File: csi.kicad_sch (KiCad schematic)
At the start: 0 parts

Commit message: Schematic cleanup
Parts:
- added J?: WE_68715014522, antmicro-footprints:WE_68715014522, symbol antmicroFCCConnectors:WE_68715014522
- added MP? (x4): PCB_Mount_Hole_4.3_NPTH, antmicro-footprints:mounting-hole-4.2mm-NPTH, symbol antmicroMechanicalParts:PCB_Mount_Hole_4.3_NPTH
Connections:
- new net +3V3: J?.47 (Pin_47), J?.48 (Pin_48)
- new net +5V: J?.49 (Pin_49), J?.50 (Pin_50)
- new net CSI1_CLK_N: J?.28 (Pin_28)
- new net CSI1_CLK_P: J?.29 (Pin_29)
- new net CSI1_D1_N: J?.25 (Pin_25)
- new net CSI1_D1_P: J?.26 (Pin_26)
- new net CSI1_D2_N: J?.23 (Pin_23)
- new net CSI1_D2_P: J?.24 (Pin_24)
- new net CSI1_D3_N: J?.21 (Pin_21)
- new net CSI1_D3_P: J?.22 (Pin_22)
- new net CSI1_D4_N: J?.19 (Pin_19)
- new net CSI1_D4_P: J?.20 (Pin_20)
- new net CSI2_CLK_N: J?.13 (Pin_13)
- new net CSI2_CLK_P: J?.14 (Pin_14)
- new net CSI2_D1_N: J?.16 (Pin_16)
- new net CSI2_D1_P: J?.17 (Pin_17)
- new net CSI3_CLK_N: J?.10 (Pin_10)
- new net CSI3_CLK_P: J?.11 (Pin_11)
- new net CSI3_D1_N: J?.7 (Pin_7)
- new net CSI3_D1_P: J?.8 (Pin_8)
- new net CSI3_D2_N: J?.5 (Pin_5)
- new net CSI3_D2_P: J?.6 (Pin_6)
- new net CSI3_D3_N: J?.3 (Pin_3)
- new net CSI3_D3_P: J?.4 (Pin_4)
- new net CSI3_D4_N: J?.1 (Pin_1)
- new net CSI3_D4_P: J?.2 (Pin_2)
- new net GND: J?.12 (Pin_12), J?.15 (Pin_15), J?.18 (Pin_18), J?.9 (Pin_9)
- new net GPIO1: J?.31 (Pin_31)
- new net GPIO2: J?.32 (Pin_32)
- new net GPIO3: J?.33 (Pin_33)
- new net GPIO4: J?.34 (Pin_34)
- new net I2C1_SCL: J?.42 (Pin_42)
- new net I2C1_SDA: J?.41 (Pin_41)
- new net I2C3_SCL: J?.40 (Pin_40)
- new net I2C3_SDA: J?.39 (Pin_39)
- new net SPI_CS: J?.46 (Pin_46)
- new net SPI_MISO: J?.44 (Pin_44)
- new net SPI_MOSI: J?.45 (Pin_45)
- new net SPI_SCK: J?.43 (Pin_43)
- new net UART3_RX: J?.36 (Pin_36)
- new net UART3_TX: J?.35 (Pin_35)
- new net UART4_RX: J?.38 (Pin_38)
- new net UART4_TX: J?.37 (Pin_37)
- no-connect marks 0 -> 16
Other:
- removed sheet CSI
- removed sheet Channel 1
- removed sheet Channel 2
- note added: "Camera board connector"
- note added: "The connector has flipped pads on the PCB"
- note added: "To make it compatible with TK1, TX1 boards"
- title: Antmicro HDMI MIPI Bridge -> (none)

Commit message: Updated components
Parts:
- removed J?: WE_68715014522, antmicro-footprints:WE_68715014522, symbol antmicroFCCConnectors:WE_68715014522
- added J6: WE_68715014022, antmicro-footprints:WE_68715014022, symbol antmicroFCCConnectors:WE_68715014022
- gave numbers to parts that had none: 4
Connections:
- net +3V3: now also J6.47 (Pin_47), J6.48 (Pin_48)
- net +5V: now also J6.49 (Pin_49), J6.50 (Pin_50)
- net CSI1_CLK_N: now also J6.28 (Pin_28)
- net CSI1_CLK_P: now also J6.29 (Pin_29)
- net CSI1_D1_N: now also J6.25 (Pin_25)
- net CSI1_D1_P: now also J6.26 (Pin_26)
- net CSI1_D2_N: now also J6.23 (Pin_23)
- net CSI1_D2_P: now also J6.24 (Pin_24)
- net CSI1_D3_N: now also J6.21 (Pin_21)
- net CSI1_D3_P: now also J6.22 (Pin_22)
- net CSI1_D4_N: now also J6.19 (Pin_19)
- net CSI1_D4_P: now also J6.20 (Pin_20)
- net CSI2_CLK_N: now also J6.13 (Pin_13)
- net CSI2_CLK_P: now also J6.14 (Pin_14)
- net CSI2_D1_N: now also J6.16 (Pin_16)
- net CSI2_D1_P: now also J6.17 (Pin_17)
- net CSI3_CLK_N: now also J6.10 (Pin_10)
- net CSI3_CLK_P: now also J6.11 (Pin_11)
- net CSI3_D1_N: now also J6.7 (Pin_7)
- net CSI3_D1_P: now also J6.8 (Pin_8)
- net CSI3_D2_N: now also J6.5 (Pin_5)
- net CSI3_D2_P: now also J6.6 (Pin_6)
- net CSI3_D3_N: now also J6.3 (Pin_3)
- net CSI3_D3_P: now also J6.4 (Pin_4)
- net CSI3_D4_N: now also J6.1 (Pin_1)
- net CSI3_D4_P: now also J6.2 (Pin_2)
- net GND: now also J6.12 (Pin_12), J6.15 (Pin_15), J6.18 (Pin_18), J6.9 (Pin_9)
- net GPIO1: now also J6.31 (Pin_31)
- net GPIO2: now also J6.32 (Pin_32)
- net GPIO3: now also J6.33 (Pin_33)
- net GPIO4: now also J6.34 (Pin_34)
- net I2C1_SCL: now also J6.42 (Pin_42)
- net I2C1_SDA: now also J6.41 (Pin_41)
- net I2C3_SCL: now also J6.40 (Pin_40)
- net I2C3_SDA: now also J6.39 (Pin_39)
- net SPI_CS: now also J6.46 (Pin_46)
- net SPI_MISO: now also J6.44 (Pin_44)
- net SPI_MOSI: now also J6.45 (Pin_45)
- net SPI_SCK: now also J6.43 (Pin_43)
- net UART3_RX: now also J6.36 (Pin_36)
- net UART3_TX: now also J6.35 (Pin_35)
- net UART4_RX: now also J6.38 (Pin_38)
- net UART4_TX: now also J6.37 (Pin_37)
- no-connect marks 16 -> 18
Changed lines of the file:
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@@
   (no_connect (at 186.69 189.23))
   (no_connect (at 186.69 113.03))
+  (no_connect (at 204.47 156.21))
+  (no_connect (at 204.47 148.59))
   (wire (pts (xy 203.2 207.01) (xy 204.47 207.01))
     (stroke (width 0) (type default) (color 0 0 0 0))
@@
     )
   )
-  (symbol (lib_id "antmicroFCCConnectors:WE_68715014522") (at 209.55 123.19 0) (unit 1)
+  (symbol (lib_id "antmicroMechanicalParts:PCB_Mount_Hole_4.3_NPTH") (at 297.18 205.74 0) (unit 1)
     (in_bom yes) (on_board yes) (fields_autoplaced)
-    (property "Reference" "J?" (id 0) (at 212.09 143.5099 0)
+    (property "Reference" "MP4" (id 0) (at 303.53 204.4699 0)
       (effects (font (size 1.27 1.27)) (justify left))
     )
-    (property "Value" "WE_68715014522" (id 1) (at 212.09 146.0499 0)
+    (property "Value" "PCB_Mount_Hole_4.3_NPTH" (id 1) (at 303.53 207.0099 0)
       (effects (font (size 1.27 1.27)) (justify left))
     )
-    (property "Footprint" "antmicro-footprints:WE_68715014522" (id 2) (at 204.47 213.36 0)
+    (property "Footprint" "antmicro-footprints:mounting-hole-4.2mm-NPTH" (id 2) (at 297.18 195.58 0)
       (effects (font (size 1.27 1.27)) hide)
     )
-    (property "Datasheet" "https://katalog.we-online.de/em/datasheet/6871xx14522.pdf" (id 3) (at 209.55 215.9 0)
+    (property "Datasheet" "" (id 3) (at 321.31 185.42 0)
       (effects (font (size 1.27 1.27)) hide)
     )
-    (property "MPN" "68715014522 " (id 4) (at 219.71 138.43 0)
+  )
+  (symbol (lib_id "antmicroMechanicalParts:PCB_Mount_Hole_4.3_NPTH") (at 259.08 205.74 0) (unit 1)
+    (in_bom yes) (on_board yes) (fields_autoplaced)
+    (property "Reference" "MP2" (id 0) (at 265.43 204.4699 0)
+      (effects (font (size 1.27 1.27)) (justify left))
+    )
+    (property "Value" "PCB_Mount_Hole_4.3_NPTH" (id 1) (at 265.43 207.0099 0)
+      (effects (font (size 1.27 1.27)) (justify left))
+    )
+    (property "Footprint" "antmicro-footprints:mounting-hole-4.2mm-NPTH" (id 2) (at 259.08 195.58 0)
+      (effects (font (size 1.27 1.27)) hide)
+    )
+    (property "Datasheet" "" (id 3) (at 283.21 185.42 0)
+      (effects (font (size 1.27 1.27)) hide)
+    )
+  )
+  (symbol (lib_id "antmicroMechanicalParts:PCB_Mount_Hole_4.3_NPTH") (at 259.08 195.58 0) (unit 1)
+    (in_bom yes) (on_board yes) (fields_autoplaced)
+    (property "Reference" "MP1" (id 0) (at 265.43 194.3099 0)
+      (effects (font (size 1.27 1.27)) (justify left))
+    )
+    (property "Value" "PCB_Mount_Hole_4.3_NPTH" (id 1) (at 265.43 196.8499 0)
+      (effects (font (size 1.27 1.27)) (justify left))
+    )
+    (property "Footprint" "antmicro-footprints:mounting-hole-4.2mm-NPTH" (id 2) (at 259.08 185.42 0)
+      (effects (font (size 1.27 1.27)) hide)
+    )
+    (property "Datasheet" "" (id 3) (at 283.21 175.26 0)
+      (effects (font (size 1.27 1.27)) hide)
+    )
+  )
+  (symbol (lib_id "power:GND") (at 201.93 209.55 0) (unit 1)
+    (in_bom yes) (on_board yes) (fields_autoplaced)
+    (property "Reference" "#PWR0101" (id 0) (at 201.93 215.9 0)
+      (effects (font (size 1.27 1.27)) hide)
+    )
+    (property "Value" "GND" (id 1) (at 201.93 214.63 0))
+    (property "Footprint" "" (id 2) (at 201.93 209.55 0)
+      (effects (font (size 1.27 1.27)) hide)
+    )
+    (property "Datasheet" "" (id 3) (at 201.93 209.55 0)
+      (effects (font (size 1.27 1.27)) hide)
+    )
+    (pin "1")
+  )
+  (symbol (lib_id "antmicroMechanicalParts:PCB_Mount_Hole_4.3_NPTH") (at 297.18 195.58 0) (unit 1)
+    (in_bom yes) (on_board yes) (fields_autoplaced)
+    (property "Reference" "MP3" (id 0) (at 303.53 194.3099 0)
+      (effects (font (size 1.27 1.27)) (justify left))
+    )
+    (property "Value" "PCB_Mount_Hole_4.3_NPTH" (id 1) (at 303.53 196.8499 0)
+      (effects (font (size 1.27 1.27)) (justify left))
+    )
+    (property "Footprint" "antmicro-footprints:mounting-hole-4.2mm-NPTH" (id 2) (at 297.18 185.42 0)
+      (effects (font (size 1.27 1.27)) hide)
+    )
+    (property "Datasheet" "" (id 3) (at 321.31 175.26 0)
+      (effects (font (size 1.27 1.27)) hide)
+    )
+  )
+  (symbol (lib_id "power:+3V3") (at 198.12 200.66 0) (unit 1)
+    (in_bom yes) (on_board yes)
+    (property "Reference" "#PWR0102" (id 0) (at 198.12 204.47 0)
+      (effects (font (size 1.27 1.27)) hide)
+    )
+    (property "Value" "+3V3" (id 1) (at 194.31 199.39 0))
+    (property "Footprint" "" (id 2) (at 198.12 200.66 0)
+      (effects (font (size 1.27 1.27)) hide)
+    )
+    (property "Datasheet" "" (id 3) (at 198.12 200.66 0)
+      (effects (font (size 1.27 1.27)) hide)
+    )
+    (pin "1")
+  )
+  (symbol (lib_id "antmicroFCCConnectors:WE_68715014022") (at 209.55 123.19 0) (unit 1)
+    (in_bom yes) (on_board yes) (fields_autoplaced)
+    (property "Reference" "J6" (id 0) (at 212.09 143.5099 0)
+      (effects (font (size 1.27 1.27)) (justify left))
+    )
+    (property "Value" "WE_68715014022" (id 1) (at 212.09 146.0499 0)
+      (effects (font (size 1.27 1.27)) (justify left))
+    )
+    (property "Footprint" "antmicro-footprints:WE_68715014022" (id 2) (at 204.47 213.36 0)
+      (effects (font (size 1.27 1.27)) hide)
+    )
+    (property "Datasheet" "" (id 3) (at 209.55 215.9 0)
+      (effects (font (size 1.27 1.27)) hide)
+    )
+    (property "MPN" "68715014022 " (id 4) (at 219.71 138.43 0)
       (effects (font (size 1.524 1.524)) (justify left) hide)
     )
@@
     (pin "9")
   )
-  (symbol (lib_id "antmicroMechanicalParts:PCB_Mount_Hole_4.3_NPTH") (at 297.18 205.74 0) (unit 1)
-    (in_bom yes) (on_board yes) (fields_autoplaced)
-    (property "Reference" "MP?" (id 0) (at 303.53 204.4699 0)
-      (effects (font (size 1.27 1.27)) (justify left))
-    )
-    (property "Value" "PCB_Mount_Hole_4.3_NPTH" (id 1) (at 303.53 207.0099 0)
-      (effects (font (size 1.27 1.27)) (justify left))
-    )
-    (property "Footprint" "antmicro-footprints:mounting-hole-4.2mm-NPTH" (id 2) (at 297.18 195.58 0)
-      (effects (font (size 1.27 1.27)) hide)
-    )
-    (property "Datasheet" "" (id 3) (at 321.31 185.42 0)
-      (effects (font (size 1.27 1.27)) hide)
-    )
-  )
-  (symbol (lib_id "antmicroMechanicalParts:PCB_Mount_Hole_4.3_NPTH") (at 259.08 205.74 0) (unit 1)
-    (in_bom yes) (on_board yes) (fields_autoplaced)
-    (property "Reference" "MP?" (id 0) (at 265.43 204.4699 0)
-      (effects (font (size 1.27 1.27)) (justify left))
-    )
-    (property "Value" "PCB_Mount_Hole_4.3_NPTH" (id 1) (at 265.43 207.0099 0)
-      (effects (font (size 1.27 1.27)) (justify left))
-    )
-    (property "Footprint" "antmicro-footprints:mounting-hole-4.2mm-NPTH" (id 2) (at 259.08 195.58 0)
-      (effects (font (size 1.27 1.27)) hide)
-    )
-    (property "Datasheet" "" (id 3) (at 283.21 185.42 0)
-      (effects (font (size 1.27 1.27)) hide)
-    )
-  )
-  (symbol (lib_id "antmicroMechanicalParts:PCB_Mount_Hole_4.3_NPTH") (at 259.08 195.58 0) (unit 1)
-    (in_bom yes) (on_board yes) (fields_autoplaced)
-    (property "Reference" "MP?" (id 0) (at 265.43 194.3099 0)
-      (effects (font (size 1.27 1.27)) (justify left))
-    )
-    (property "Value" "PCB_Mount_Hole_4.3_NPTH" (id 1) (at 265.43 196.8499 0)
-      (effects (font (size 1.27 1.27)) (justify left))
-    )
-    (property "Footprint" "antmicro-footprints:mounting-hole-4.2mm-NPTH" (id 2) (at 259.08 185.42 0)
-      (effects (font (size 1.27 1.27)) hide)
-    )
-    (property "Datasheet" "" (id 3) (at 283.21 175.26 0)
-      (effects (font (size 1.27 1.27)) hide)
-    )
-  )
-  (symbol (lib_id "power:GND") (at 201.93 209.55 0) (unit 1)
-    (in_bom yes) (on_board yes) (fields_autoplaced)
-    (property "Reference" "#PWR?" (id 0) (at 201.93 215.9 0)
-      (effects (font (size 1.27 1.27)) hide)
-    )
-    (property "Value" "GND" (id 1) (at 201.93 214.63 0))
-    (property "Footprint" "" (id 2) (at 201.93 209.55 0)
-      (effects (font (size 1.27 1.27)) hide)
-    )
-    (property "Datasheet" "" (id 3) (at 201.93 209.55 0)
-      (effects (font (size 1.27 1.27)) hide)
-    )
-    (pin "1")
-  )
-  (symbol (lib_id "antmicroMechanicalParts:PCB_Mount_Hole_4.3_NPTH") (at 297.18 195.58 0) (unit 1)
-    (in_bom yes) (on_board yes) (fields_autoplaced)
-    (property "Reference" "MP?" (id 0) (at 303.53 194.3099 0)
-      (effects (font (size 1.27 1.27)) (justify left))
-    )
-    (property "Value" "PCB_Mount_Hole_4.3_NPTH" (id 1) (at 303.53 196.8499 0)
-      (effects (font (size 1.27 1.27)) (justify left))
-    )
-    (property "Footprint" "antmicro-footprints:mounting-hole-4.2mm-NPTH" (id 2) (at 297.18 185.42 0)
-      (effects (font (size 1.27 1.27)) hide)
-    )
-    (property "Datasheet" "" (id 3) (at 321.31 175.26 0)
-      (effects (font (size 1.27 1.27)) hide)
-    )
-  )
-  (symbol (lib_id "power:+3V3") (at 198.12 200.66 0) (unit 1)
-    (in_bom yes) (on_board yes)
-    (property "Reference" "#PWR?" (id 0) (at 198.12 204.47 0)
-      (effects (font (size 1.27 1.27)) hide)
-    )
-    (property "Value" "+3V3" (id 1) (at 194.31 199.39 0))
-    (property "Footprint" "" (id 2) (at 198.12 200.66 0)
-      (effects (font (size 1.27 1.27)) hide)
-    )
-    (property "Datasheet" "" (id 3) (at 198.12 200.66 0)
-      (effects (font (size 1.27 1.27)) hide)
-    )
-    (pin "1")
-  )
   (symbol (lib_id "power:+5V") (at 198.12 205.74 0) (unit 1)
     (in_bom yes) (on_board yes)
-    (property "Reference" "#PWR?" (id 0) (at 198.12 209.55 0)
+    (property "Reference" "#PWR0103" (id 0) (at 198.12 209.55 0)
       (effects (font (size 1.27 1.27)) hide)
     )

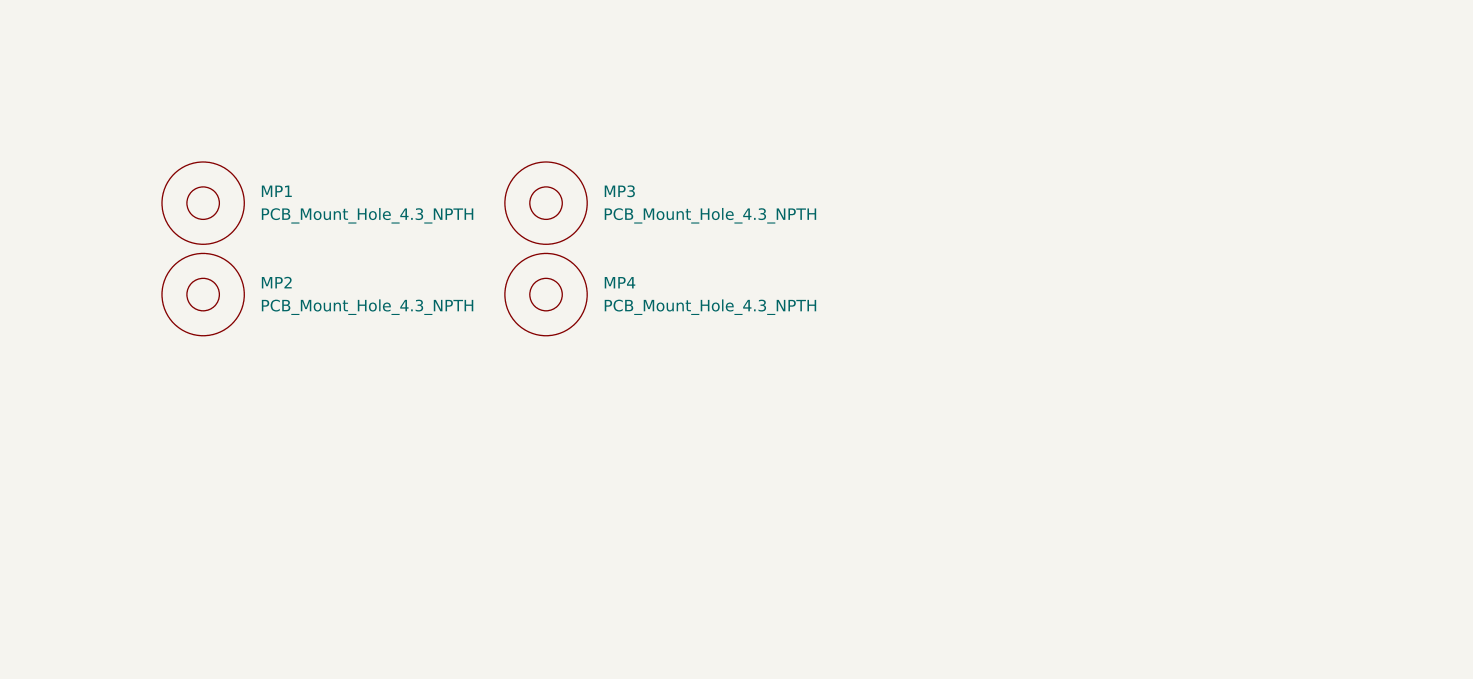
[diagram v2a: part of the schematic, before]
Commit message: Changed mounting holes to stubs
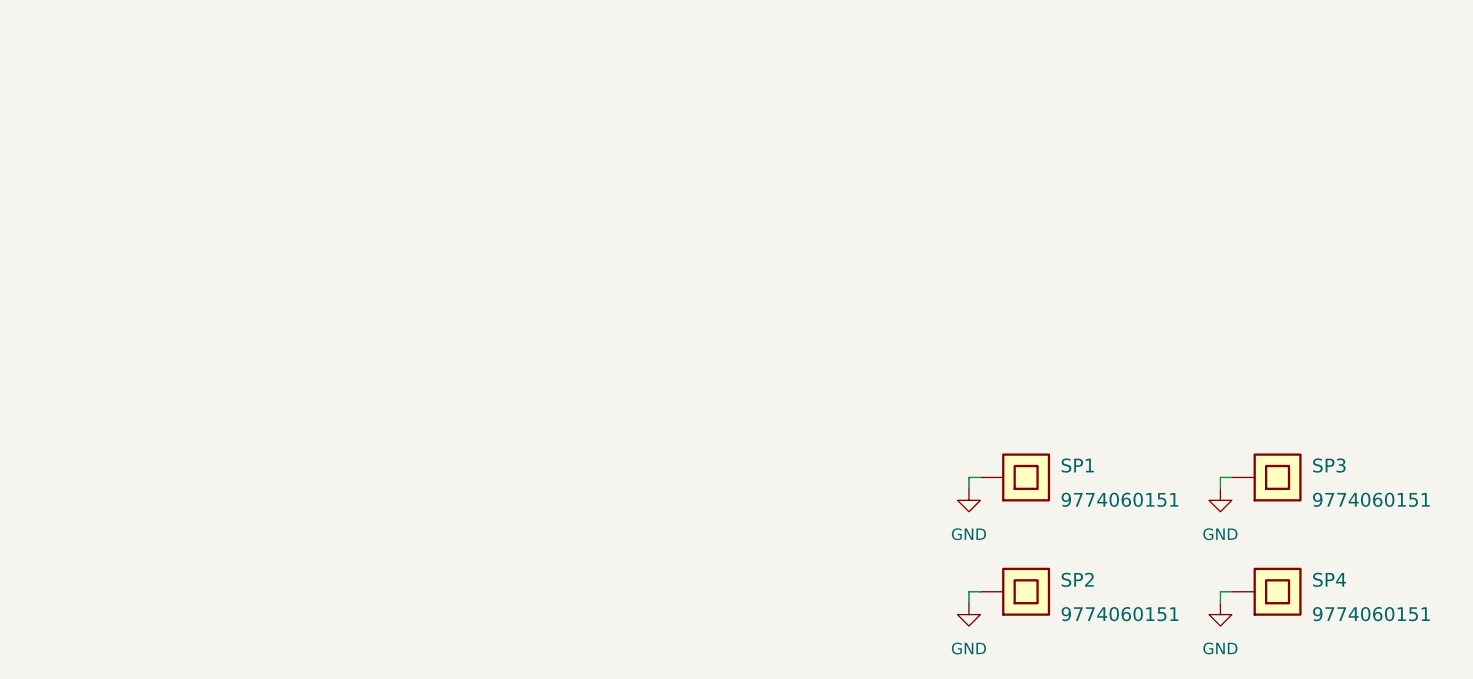
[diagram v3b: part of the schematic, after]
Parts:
- removed MP1, MP2, MP3, MP4: PCB_Mount_Hole_4.3_NPTH, antmicro-footprints:mounting-hole-4.2mm-NPTH, symbol antmicroMechanicalParts:PCB_Mount_Hole_4.3_NPTH
- added SP1, SP2, SP3, SP4: 9774060151, antmicro-footprints:9774060151, symbol antmicroMechanicalParts:9774060151
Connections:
- net GND: now also SP1.1, SP2.1, SP3.1, SP4.1

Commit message: Update local library of components
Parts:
- J6: footprint antmicro-footprints:WE_68715014022 -> antmicro-hdmi-mipi-bridge-hw-footprints:WE_68715014022; symbol antmicroFCCConnectors:WE_68715014022 -> antmicro-hdmi-mipi-bridge-hw:WE_68715014022
- SP1, SP2, SP3, SP4: footprint antmicro-footprints:9774060151 -> antmicro-hdmi-mipi-bridge-hw-footprints:9774060151; symbol antmicroMechanicalParts:9774060151 -> antmicro-hdmi-mipi-bridge-hw:9774060151
